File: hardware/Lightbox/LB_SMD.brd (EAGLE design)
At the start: 90 x 60 mm, 36 parts, among them Q1 8MHz, Q2 IRLZ44Z, Q3 IRLZ44Z, Q4 IRLZ44Z, SW1 NT-10 SMD, U1 ATTiny2313, U2 75176, U3 LM1117-5.0

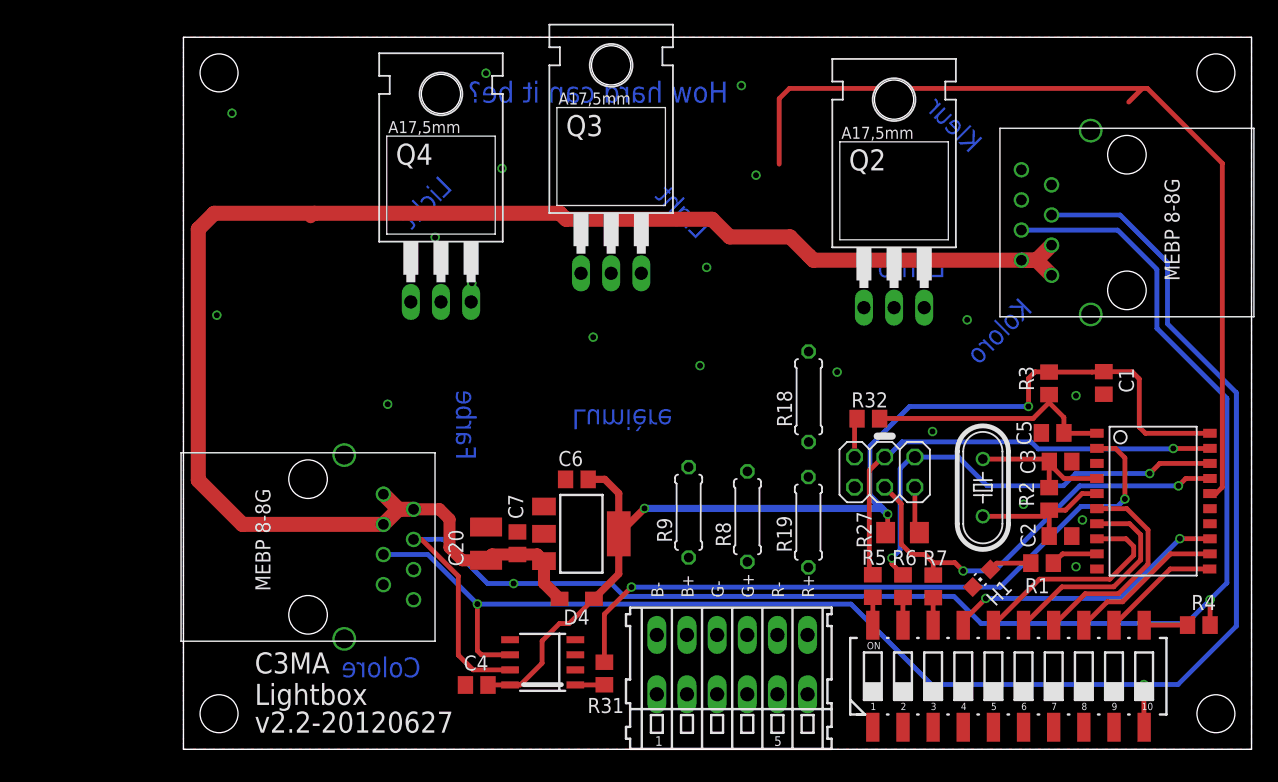
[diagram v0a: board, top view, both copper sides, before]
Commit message: removed parts of old routing from PCB
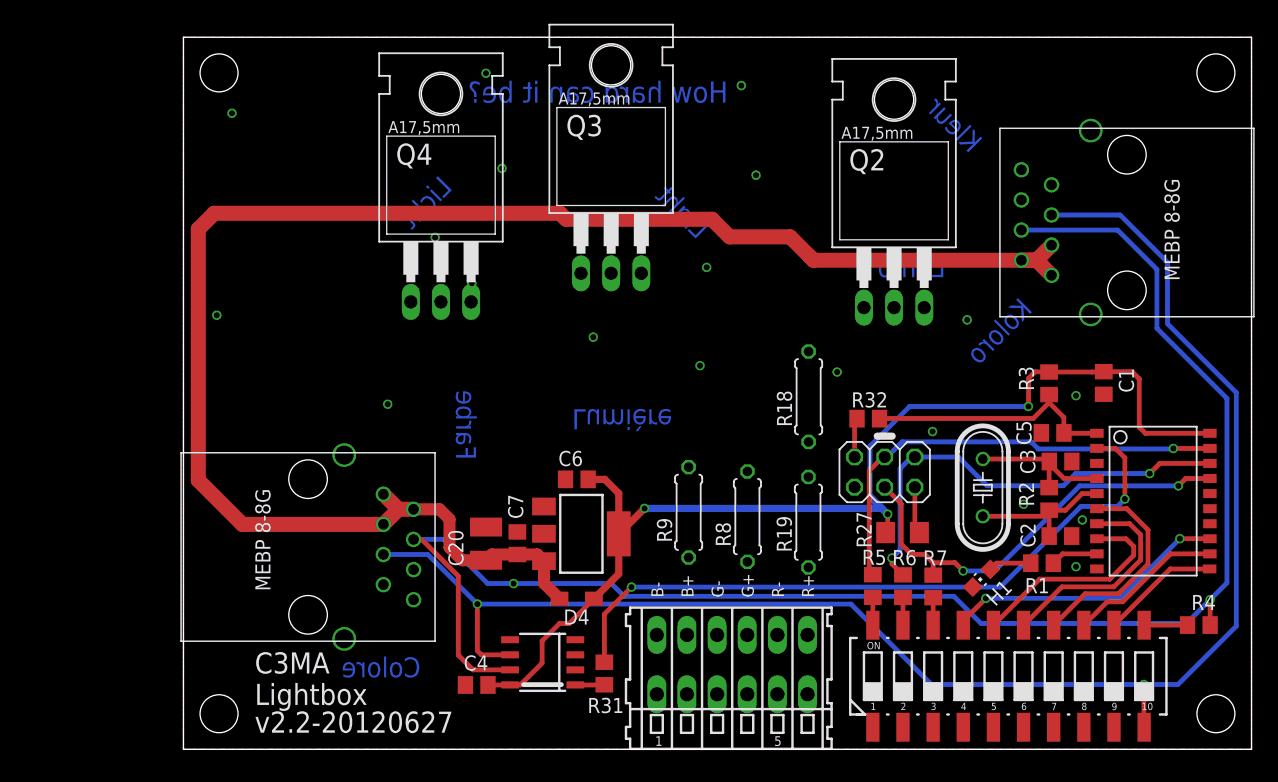
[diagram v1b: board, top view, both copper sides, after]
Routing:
- net N$33: track 76.0 -> 0.00 mm
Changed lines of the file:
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@@
 <wire x1="46.03" y1="43.18" x2="45.94" y2="43.18" width="1.016" layer="1"/>
 <wire x1="32.225" y1="44.665" x2="32.275" y2="44.665" width="1.016" layer="1"/>
-<wire x1="2.59" y1="45.17" x2="11.06" y2="45.17" width="1.27" layer="1"/>
-<wire x1="11.06" y1="45.17" x2="10.725" y2="44.835" width="1.016" layer="1"/>
 <wire x1="32.275" y1="44.665" x2="44.545" y2="44.665" width="1.27" layer="1"/>
 <wire x1="44.545" y1="44.665" x2="46.03" y2="43.18" width="1.27" layer="1"/>
-<wire x1="11.06" y1="45.17" x2="31.72" y2="45.17" width="1.27" layer="1"/>
+<wire x1="2.59" y1="45.17" x2="31.72" y2="45.17" width="1.27" layer="1"/>
 <wire x1="31.72" y1="45.17" x2="32.225" y2="44.665" width="1.27" layer="1"/>
 <wire x1="51.12" y1="43.18" x2="52.72" y2="41.58" width="1.27" layer="1"/>
@@
 <signal name="N$33">
 <contactref element="U1" pad="16"/>
-<wire x1="87.54" y1="49.38" x2="87.54" y2="22.09" width="0.4064" layer="1"/>
-<wire x1="81.23" y1="55.69" x2="87.54" y2="49.38" width="0.4064" layer="1"/>
-<wire x1="87.54" y1="22.09" x2="87" y2="21.55" width="0.4064" layer="1"/>
-<wire x1="87" y1="21.55" x2="86.4942" y2="21.55" width="0.4064" layer="1"/>
-<wire x1="50.2" y1="49.31" x2="50.2" y2="54.83" width="0.4064" layer="1"/>
-<wire x1="51.06" y1="55.69" x2="80.8" y2="55.69" width="0.4064" layer="1"/>
-<wire x1="80.8" y1="55.69" x2="81.23" y2="55.69" width="0.4064" layer="1"/>
-<wire x1="50.2" y1="54.83" x2="51.06" y2="55.69" width="0.4064" layer="1"/>
-<wire x1="80.8" y1="55.69" x2="79.65" y2="54.54" width="0.4064" layer="1"/>
 <contactref element="Q2" pad="G"/>
-<wire x1="57.34" y1="37.22" x2="50.2" y2="49.31" width="0" layer="19" extent="1-1"/>
+<wire x1="57.34" y1="37.22" x2="86.4942" y2="21.55" width="0" layer="19" extent="1-1"/>
 </signal>
 <signal name="N$53">

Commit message: changes towards THT layout
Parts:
- removed C20: 10u, LB:C1210
- removed C7: 100n, rcl:C0805
- removed D4: (no value), diode:SOD323-W
- removed H1: (no value), led:CHIP-LED0805
- removed R1: 470R, rcl:R0805
- removed R2: 1M, rcl:R0805
- removed U1: ATTiny2313, LB:SO20L
- C6: value 100n -> 100u
- U3: value LM1117-5.0 -> ATTINY2313-20PU; device v-reg:SOT223 -> lightbox:DIP254P762X533-20
- moved U3 40.8 mm to (-5.00, 4.80), turned to 0 degrees
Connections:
- removed net N$1: R1.1, U1.9
- removed net N$18: SW1.12, U1.11
- removed net N$33: Q2.G, U1.16
- removed net N$53: R31.2, U1.2
- new net N$26: Q2.G, U3.16
- new net N$27: C2.1, Q1.1, U3.5
- new net N$29: C3.1, Q1.2, U3.4
- net +12V: no longer C20.1, C7.1, D4.C, U3.3
- net +5V: now also R3.1, U3.20; no longer D4.A, R3.2, U1.20, U3.4
- net GND: now also U3.10; no longer C20.2, C7.2, H1.C, U1.10, U3.1
- net MISO: now also U3.18; no longer U1.18
- net MOSI: now also U3.17; no longer U1.17
- net N$11: now also U3.15; no longer U1.15
- net N$13: now also U3.13; no longer U1.13
- net N$14: now also U3.8; no longer U1.8
- net N$15: now also U3.7; no longer U1.7
- net N$16: now also U3.6; no longer U1.6
- net N$17: now also U3.2; no longer SW1.13, U1.12
- net N$19: now also U3.14; no longer U1.14
- net N$2: now also R3.2, U3.1; no longer C2.1, Q1.2, R2.1, U1.5
- net N$3: now also SW1.12, U3.11; no longer H1.A, R1.2
- net N$4: now also SW1.13, U3.12; no longer C3.1, Q1.1, R2.2, U1.4
- net N$6: no longer R3.1, U1.1
- net SCK: now also U3.19; no longer U1.19
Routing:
- net +12V: track 139.3 -> 0.00 mm
- net DMX_A: track 133.4 -> 0.00 mm, vias 2 -> 0
- net DMX_B: track 133.3 -> 0.00 mm, vias 2 -> 0
- net +5V: track 94.8 -> 0.00 mm, vias 3 -> 0
- net N$53: track 58.1 -> 0.00 mm, vias 2 -> 0
- net SCK: track 38.9 -> 0.00 mm, vias 1 -> 0
- net MISO: track 37.9 -> 0.00 mm, vias 2 -> 0
- net MOSI: track 36.6 -> 0.00 mm, vias 2 -> 0
- net N$13: track 24.0 -> 0.00 mm, vias 2 -> 0
- net N$6: track 21.4 -> 0.00 mm
- net N$14: track 18.4 -> 0.00 mm
- net N$15: track 18.3 -> 0.00 mm
- net N$16: track 18.0 -> 0.00 mm
- net N$17: track 13.1 -> 0.00 mm
- net N$2: track 12.9 -> 0.00 mm
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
